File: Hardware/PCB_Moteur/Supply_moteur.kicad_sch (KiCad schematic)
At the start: 26 parts, among them J15 Vin_XT30PW-F, U13 L6981N33DR

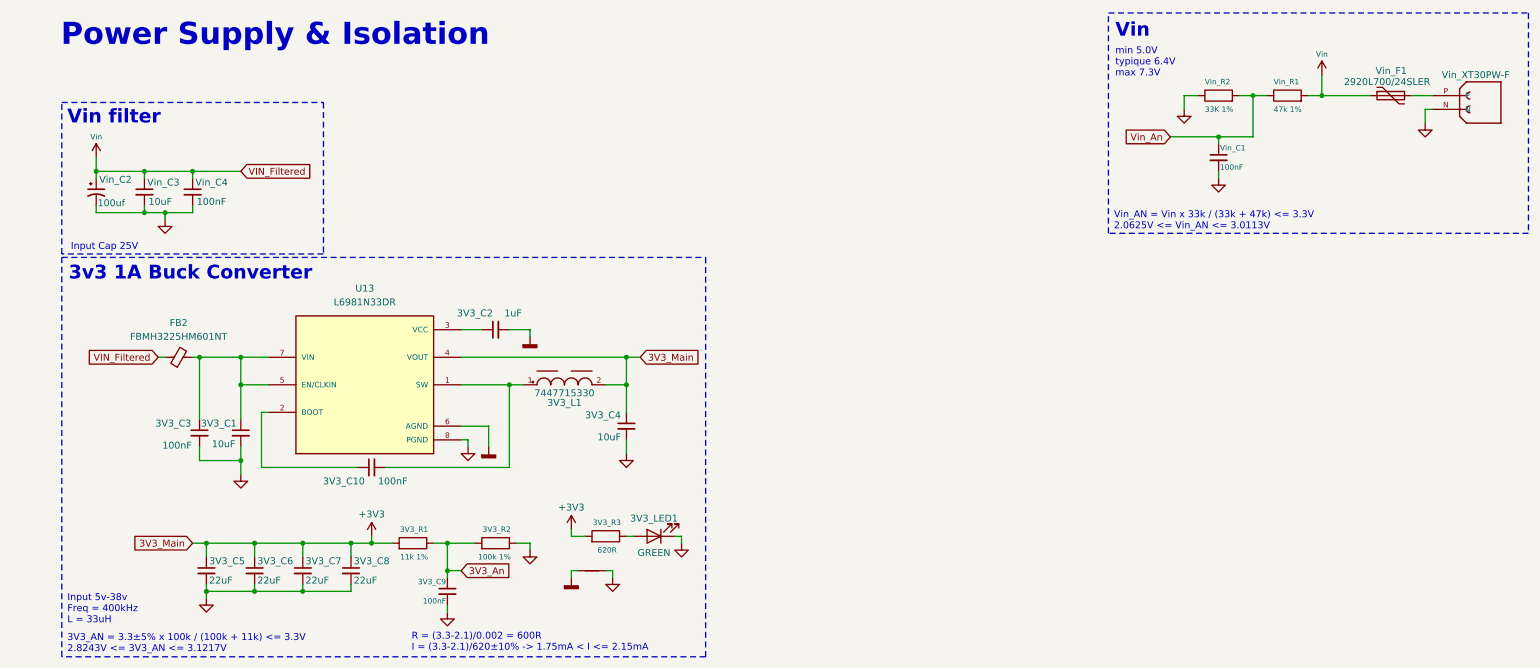
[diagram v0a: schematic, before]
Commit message: fix: LDO 5V SHDN + REFs (missing) + change EN valves controller connection + fix intrumental ampliop + add pull-down to sleep pins
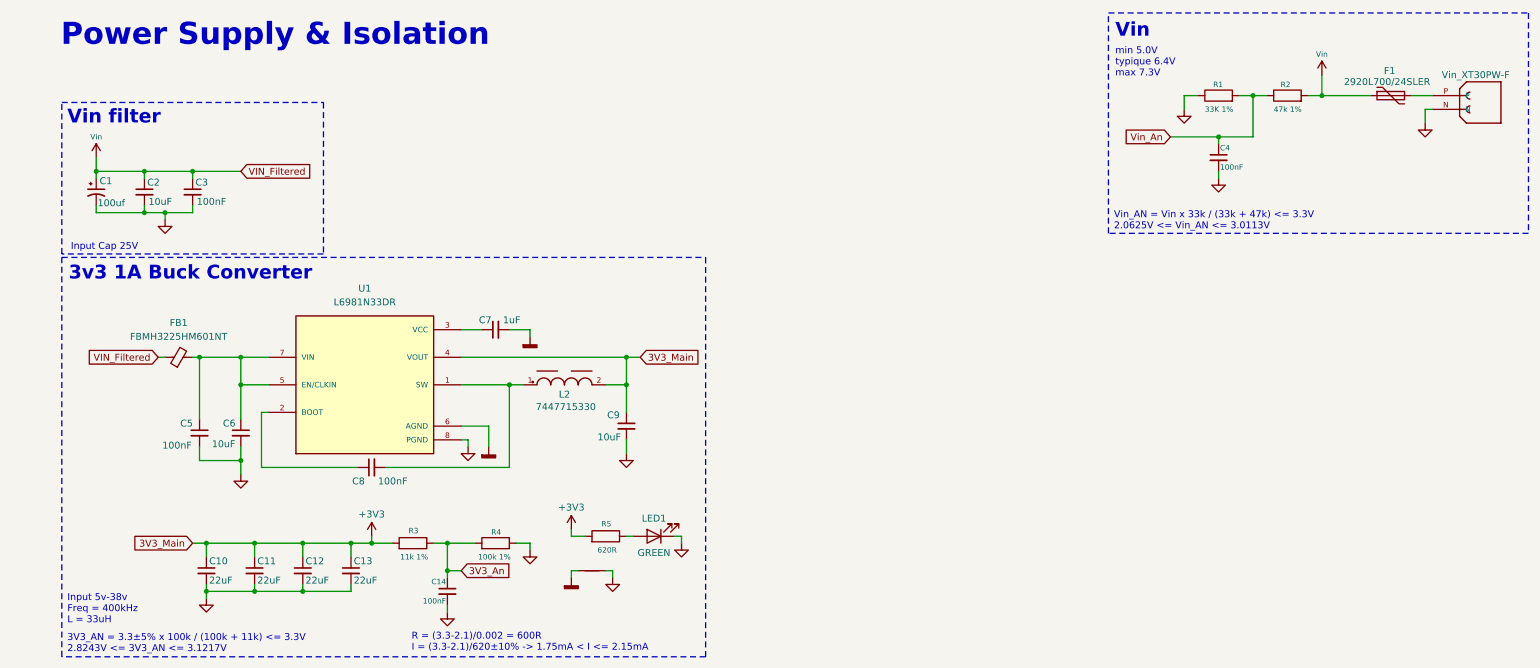
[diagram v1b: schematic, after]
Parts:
- renumbered Vin_C2 to C1, 3V3_C5 to C10, 3V3_C6 to C11, 3V3_C7 to C12, 3V3_C8 to C13, 3V3_C9 to C14, Vin_C3 to C2, Vin_C4 to C3, Vin_C1 to C4, 3V3_C3 to C5, 3V3_C1 to C6, 3V3_C2 to C7, 3V3_C10 to C8, 3V3_C4 to C9, Vin_F1 to F1, FB2 to FB1, J15 to J1, 3V3_L1 to L2, 3V3_LED1 to LED1, Vin_R2 to R1, Vin_R1 to R2, 3V3_R1 to R3, 3V3_R2 to R4, 3V3_R3 to R5, U13 to U1
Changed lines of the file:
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@@
 		(on_board yes)
 		(dnp no)
-		(property "Reference" "3V3_R2"
-			(at 96.774 107.95 90)
+		(property "Reference" "R4"
+			(at 94.996 108.458 90)
 			(effects
 				(font
@@
 			(project "PCB_moteur"
 				(path "/b0d87684-7b1c-41d8-8358-755aa327573e/92d1df5d-a307-4eea-a65c-ade4cb0ad548"
-					(reference "3V3_R2")
+					(reference "R4")
 					(unit 1)
 				)
@@
 		(on_board yes)
 		(dnp no)
-		(property "Reference" "3V3_C6"
+		(property "Reference" "C11"
 			(at 50.038 113.792 0)
 			(effects
@@
 			(project "PCB_moteur"
 				(path "/b0d87684-7b1c-41d8-8358-755aa327573e/92d1df5d-a307-4eea-a65c-ade4cb0ad548"
-					(reference "3V3_C6")
+					(reference "C11")
 					(unit 1)
 				)
@@
 		(on_board yes)
 		(dnp no)
-		(property "Reference" "3V3_R1"
-			(at 81.534 107.95 90)
+		(property "Reference" "R3"
+			(at 79.756 108.204 90)
 			(effects
 				(font
@@
 			(project "PCB_moteur"
 				(path "/b0d87684-7b1c-41d8-8358-755aa327573e/92d1df5d-a307-4eea-a65c-ade4cb0ad548"
-					(reference "3V3_R1")
+					(reference "R3")
 					(unit 1)
 				)
@@
 		(on_board yes)
 		(dnp no)
-		(property "Reference" "3V3_C1"
-			(at 39.624 88.392 0)
+		(property "Reference" "C6"
+			(at 43.688 88.392 0)
 			(effects
 				(font
@@
 			(project "PCB_moteur"
 				(path "/b0d87684-7b1c-41d8-8358-755aa327573e/92d1df5d-a307-4eea-a65c-ade4cb0ad548"
-					(reference "3V3_C1")
+					(reference "C6")
 					(unit 1)
 				)
@@
 		(on_board yes)
 		(dnp no)
-		(property "Reference" "3V3_C2"
-			(at 93.472 68.072 90)
+		(property "Reference" "C7"
+			(at 93.218 69.342 90)
 			(effects
 				(font
@@
 		)
 		(property "Value" "1uF"
-			(at 98.806 68.072 90)
+			(at 98.552 69.342 90)
 			(effects
 				(font
@@
 			(project "PCB_moteur"
 				(path "/b0d87684-7b1c-41d8-8358-755aa327573e/92d1df5d-a307-4eea-a65c-ade4cb0ad548"
-					(reference "3V3_C2")
+					(reference "C7")
 					(unit 1)
 				)
@@
 		(on_board yes)
 		(dnp no)
-		(property "Reference" "3V3_L1"
-			(at 106.68 84.582 0)
+		(property "Reference" "L2"
+			(at 106.68 83.058 0)
 			(effects
 				(font
@@
 		)
 		(property "Value" "7447715330"
-			(at 106.68 82.804 0)
+			(at 106.934 85.344 0)
 			(effects
 				(font
@@
 			(project "PCB_moteur"
 				(path "/b0d87684-7b1c-41d8-8358-755aa327573e/92d1df5d-a307-4eea-a65c-ade4cb0ad548"
-					(reference "3V3_L1")
+					(reference "L2")
 					(unit 1)
 				)
@@
 		(on_board yes)
 		(dnp no)
-		(property "Reference" "3V3_R3"
-			(at 117.094 106.68 90)
+		(property "Reference" "R5"
+			(at 115.316 106.934 90)
 			(effects
 				(font
@@
 			(project "PCB_moteur"
 				(path "/b0d87684-7b1c-41d8-8358-755aa327573e/92d1df5d-a307-4eea-a65c-ade4cb0ad548"
-					(reference "3V3_R3")
+					(reference "R5")
 					(unit 1)
 				)
@@
 		(on_board yes)
 		(dnp no)
-		(property "Reference" "Vin_C2"
-			(at 23.876 43.434 0)
+		(property "Reference" "C1"
+			(at 22.098 43.688 0)
 			(effects
 				(font
@@
 			(project "PCB_moteur"
 				(path "/b0d87684-7b1c-41d8-8358-755aa327573e/92d1df5d-a307-4eea-a65c-ade4cb0ad548"
-					(reference "Vin_C2")
+					(reference "C1")
 					(unit 1)
 				)
@@
 		(on_board yes)
 		(dnp no)
-		(property "Reference" "3V3_LED1"
+		(property "Reference" "LED1"
 			(at 123.19 105.918 0)
 			(effects
@@
 			(project "PCB_moteur"
 				(path "/b0d87684-7b1c-41d8-8358-755aa327573e/92d1df5d-a307-4eea-a65c-ade4cb0ad548"
-					(reference "3V3_LED1")
+					(reference "LED1")
 					(unit 1)
 				)
@@
 		(on_board yes)
 		(dnp no)
-		(property "Reference" "Vin_R2"
-			(at 224.79 25.4 90)
+		(property "Reference" "R1"
+			(at 226.314 25.908 90)
 			(effects
 				(font
@@
 			(project "PCB_moteur"
 				(path "/b0d87684-7b1c-41d8-8358-755aa327573e/92d1df5d-a307-4eea-a65c-ade4cb0ad548"
-					(reference "Vin_R2")
+					(reference "R1")
 					(unit 1)
 				)
@@
 		(on_board yes)
 		(dnp no)
-		(property "Reference" "3V3_C5"
+		(property "Reference" "C10"
 			(at 41.148 113.792 0)
 			(effects
@@
 			(project "PCB_moteur"
 				(path "/b0d87684-7b1c-41d8-8358-755aa327573e/92d1df5d-a307-4eea-a65c-ade4cb0ad548"
-					(reference "3V3_C5")
+					(reference "C10")
 					(unit 1)
 				)
@@
 		(on_board yes)
 		(dnp no)
-		(property "Reference" "Vin_F1"
-			(at 256.286 23.368 90)
+		(property "Reference" "F1"
+			(at 257.81 23.368 90)
 			(effects
 				(font
@@
 			(project "PCB_moteur"
 				(path "/b0d87684-7b1c-41d8-8358-755aa327573e/92d1df5d-a307-4eea-a65c-ade4cb0ad548"
-					(reference "Vin_F1")
+					(reference "F1")
 					(unit 1)
 				)
@@
 		(dnp no)
 		(fields_autoplaced yes)
-		(property "Reference" "U13"
+		(property "Reference" "U1"
 			(at 69.85 63.5 0)
 			(effects
@@
 			(project "PCB_moteur"
 				(path "/b0d87684-7b1c-41d8-8358-755aa327573e/92d1df5d-a307-4eea-a65c-ade4cb0ad548"
-					(reference "U13")
+					(reference "U1")
 					(unit 1)
 				)
@@
 		(on_board yes)
 		(dnp no)
-		(property "Reference" "Vin_R1"
-			(at 237.49 25.4 90)
+		(property "Reference" "R2"
+			(at 238.76 25.908 90)
 			(effects
 				(font
@@
 			(project "PCB_moteur"
 				(path "/b0d87684-7b1c-41d8-8358-755aa327573e/92d1df5d-a307-4eea-a65c-ade4cb0ad548"
-					(reference "Vin_R1")
+					(reference "R2")
 					(unit 1)
 				)
@@
 		(on_board yes)
 		(dnp no)
-		(property "Reference" "3V3_C9"
+		(property "Reference" "C14"
 			(at 84.836 117.602 0)
 			(effects
@@
 			(project "PCB_moteur"
 				(path "/b0d87684-7b1c-41d8-8358-755aa327573e/92d1df5d-a307-4eea-a65c-ade4cb0ad548"
-					(reference "3V3_C9")
+					(reference "C14")
 					(unit 1)
 				)
@@
 		(on_board yes)
 		(dnp no)
-		(property "Reference" "Vin_C1"
+		(property "Reference" "C4"
 			(at 227.584 37.592 0)
 			(effects
@@
 			(project "PCB_moteur"
 				(path "/b0d87684-7b1c-41d8-8358-755aa327573e/92d1df5d-a307-4eea-a65c-ade4cb0ad548"
-					(reference "Vin_C1")
+					(reference "C4")
 					(unit 1)
 				)
@@
 		(on_board yes)
 		(dnp no)
-		(property "Reference" "3V3_C4"
-			(at 110.49 86.868 0)
+		(property "Reference" "C9"
+			(at 114.554 86.868 0)
 			(effects
 				(font
@@
 			(project "PCB_moteur"
 				(path "/b0d87684-7b1c-41d8-8358-755aa327573e/92d1df5d-a307-4eea-a65c-ade4cb0ad548"
-					(reference "3V3_C4")
+					(reference "C9")
 					(unit 1)
 				)
@@
 		(on_board yes)
 		(dnp no)
-		(property "Reference" "Vin_C3"
+		(property "Reference" "C2"
 			(at 29.718 43.942 0)
 			(effects
@@
 			(project "PCB_moteur"
 				(path "/b0d87684-7b1c-41d8-8358-755aa327573e/92d1df5d-a307-4eea-a65c-ade4cb0ad548"
-					(reference "Vin_C3")
+					(reference "C2")
 					(unit 1)
 				)
@@
 		(on_board yes)
 		(dnp no)
-		(property "Reference" "J15"
+		(property "Reference" "J1"
 			(at 280.67 27.9399 0)
 			(effects
@@
 			(project "PCB_moteur"
 				(path "/b0d87684-7b1c-41d8-8358-755aa327573e/92d1df5d-a307-4eea-a65c-ade4cb0ad548"
-					(reference "J15")
+					(reference "J1")
 					(unit 1)
 				)
@@
 		(dnp no)
 		(fields_autoplaced yes)
-		(property "Reference" "FB2"
+		(property "Reference" "FB1"
 			(at 35.5219 69.85 90)
 			(effects
@@
 			(project "PCB_moteur"
 				(path "/b0d87684-7b1c-41d8-8358-755aa327573e/92d1df5d-a307-4eea-a65c-ade4cb0ad548"
-					(reference "FB2")
+					(reference "FB1")
 					(unit 1)
 				)
@@
 		(on_board yes)
 		(dnp no)
-		(property "Reference" "3V3_C10"
+		(property "Reference" "C8"
 			(at 69.85 99.06 90)
 			(effects
@@
 			(project "PCB_moteur"
 				(path "/b0d87684-7b1c-41d8-8358-755aa327573e/92d1df5d-a307-4eea-a65c-ade4cb0ad548"
-					(reference "3V3_C10")
+					(reference "C8")
 					(unit 1)
 				)
@@
 		(on_board yes)
 		(dnp no)
-		(property "Reference" "3V3_C3"
-			(at 31.242 88.392 0)
+		(property "Reference" "C5"
+			(at 35.814 88.392 0)
 			(effects
 				(font
@@
 			(project "PCB_moteur"
 				(path "/b0d87684-7b1c-41d8-8358-755aa327573e/92d1df5d-a307-4eea-a65c-ade4cb0ad548"
-					(reference "3V3_C3")
+					(reference "C5")
 					(unit 1)
 				)
@@
 		(on_board yes)
 		(dnp no)
-		(property "Reference" "Vin_C4"
+		(property "Reference" "C3"
 			(at 38.608 43.942 0)
 			(effects
@@
 			(project "PCB_moteur"
 				(path "/b0d87684-7b1c-41d8-8358-755aa327573e/92d1df5d-a307-4eea-a65c-ade4cb0ad548"
-					(reference "Vin_C4")
+					(reference "C3")
 					(unit 1)
 				)
@@
 		(on_board yes)
 		(dnp no)
-		(property "Reference" "3V3_C7"
+		(property "Reference" "C12"
 			(at 58.928 113.792 0)
 			(effects
@@
 			(project "PCB_moteur"
 				(path "/b0d87684-7b1c-41d8-8358-755aa327573e/92d1df5d-a307-4eea-a65c-ade4cb0ad548"
-					(reference "3V3_C7")
+					(reference "C12")
 					(unit 1)
 				)
@@
 		(on_board yes)
 		(dnp no)
-		(property "Reference" "3V3_C8"
+		(property "Reference" "C13"
 			(at 67.818 113.792 0)
 			(effects
@@
 			(project "PCB_moteur"
 				(path "/b0d87684-7b1c-41d8-8358-755aa327573e/92d1df5d-a307-4eea-a65c-ade4cb0ad548"
-					(reference "3V3_C8")
+					(reference "C13")
 					(unit 1)
 				)

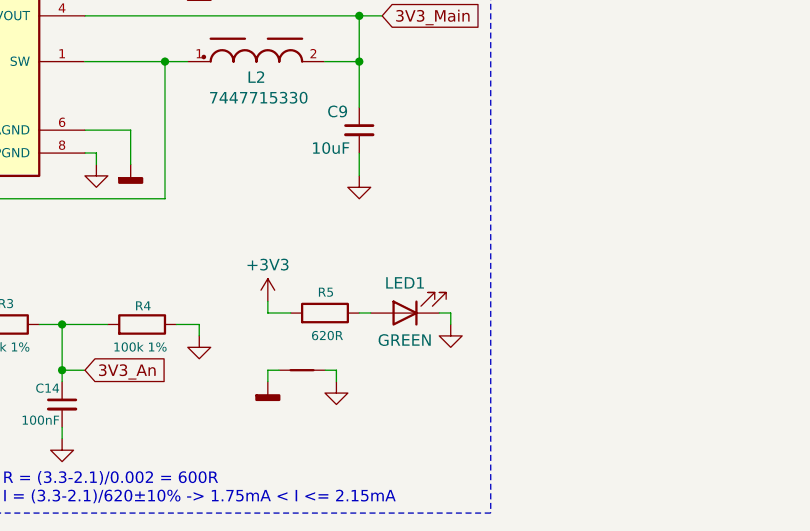
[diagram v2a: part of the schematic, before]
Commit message: wip : minor corrections and fix footprints except connectors
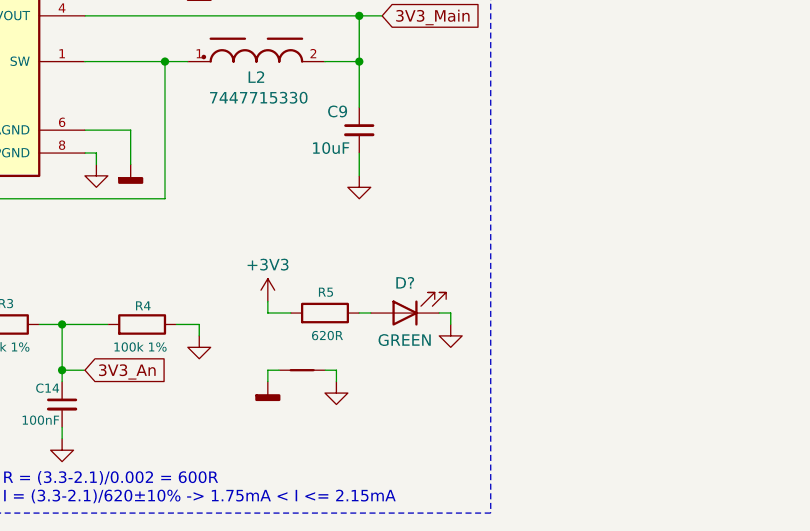
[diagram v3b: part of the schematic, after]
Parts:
- removed LED1: GREEN, LED_SMD:LED_0603_1608Metric, symbol Device:LED
- added D?: GREEN, ODB:LED_QBLP601-AG15, symbol Device:LED
- C1: footprint ODB:WCAP-PSHP_8X8.7_DXL_ -> pcb_moteur:WCAP-PSHP_8X8.7_DXL_
- C14, C3, C4, C5, C6, C7, C8: footprint Capacitor_SMD:C_0603_1608Metric -> Capacitor_SMD:C_0805_2012Metric
- C2, C9: footprint Capacitor_SMD:C_1210_3225Metric -> Capacitor_SMD:C_0805_2012Metric
- L2: footprint ODB:WE-PD_1245 -> pcb_moteur:WE-PD_1245
- U1: footprint ODB:SOIC127P600X175-8N -> pcb_moteur:SOIC127P600X175-8N
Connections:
- net GND: now also D?.1 (K)
- net at R5.1: now also D?.2 (A)
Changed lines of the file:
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@@
+	)
+	(symbol
+		(lib_id "Device:LED")
+		(at 123.19 109.22 180)
+		(unit 1)
+		(exclude_from_sim no)
+		(in_bom yes)
+		(on_board yes)
+		(dnp no)
+		(property "Reference" "D?"
+			(at 123.19 105.918 0)
+			(effects
+				(font
+					(size 1.27 1.27)
+				)
+			)
+		)
+		(property "Value" "GREEN"
+			(at 123.19 112.268 0)
+			(effects
+				(font
+					(size 1.27 1.27)
+				)
+			)
+		)
+		(property "Footprint" "ODB:LED_QBLP601-AG15"
+			(at 123.19 109.22 0)
+			(effects
+				(font
+					(size 1.27 1.27)
+				)
+				(hide yes)
+			)
+		)
+		(property "Datasheet" "https://www.digikey.ca/en/products/detail/qt-brightek-qtb/QBLP601-AG15/16499667"
+			(at 123.19 109.22 0)
+			(effects
+				(font
+					(size 1.27 1.27)
+				)
+				(hide yes)
+			)
+		)
+		(property "Description" "Light emitting diode"
+			(at 123.19 109.22 0)
+			(effects
+				(font
+					(size 1.27 1.27)
+				)
+				(hide yes)
+			)
+		)
+		(property "DigiKey_Part_Number" "1516-QBLP601-AG15CT-ND"
+			(at 123.19 109.22 0)
+			(effects
+				(font
+					(size 1.27 1.27)
+				)
+				(hide yes)
+			)
+		)
+		(property "Purchase-URL" ""
+			(at 123.19 109.22 0)
+			(effects
+				(font
+					(size 1.27 1.27)
+				)
+				(hide yes)
+			)
+		)
+		(property "Sim.Device" ""
+			(at 123.19 109.22 0)
+			(effects
+				(font
+					(size 1.27 1.27)
+				)
+				(hide yes)
+			)
+		)
+		(property "Sim.Pins" ""
+			(at 123.19 109.22 0)
+			(effects
+				(font
+					(size 1.27 1.27)
+				)
+				(hide yes)
+			)
+		)
+		(property "Sim.Type" ""
+			(at 123.19 109.22 0)
+			(effects
+				(font
+					(size 1.27 1.27)
+				)
+				(hide yes)
+			)
+		)
+		(property "Manufacturer_Part_Number" "QBLP601-AG15"
+			(at 123.19 109.22 0)
+			(effects
+				(font
+					(size 1.27 1.27)
+				)
+				(hide yes)
+			)
+		)
+		(pin "1"
+		)
+		(pin "2"
+		)
+		(instances
+			(project "PCB_moteur"
+				(path "/b0d87684-7b1c-41d8-8358-755aa327573e/92d1df5d-a307-4eea-a65c-ade4cb0ad548"
+					(reference "D?")
+					(unit 1)
+				)
+			)
+		)
 	)
 	(symbol
@@
 			)
 		)
-		(property "Footprint" "Capacitor_SMD:C_0603_1608Metric"
+		(property "Footprint" "Capacitor_SMD:C_0805_2012Metric"
 			(at 46.99 90.17 0)
 			(effects
@@
 			)
 		)
-		(property "Footprint" "Capacitor_SMD:C_0603_1608Metric"
+		(property "Footprint" "Capacitor_SMD:C_0805_2012Metric"
 			(at 93.98 71.12 0)
 			(effects
@@
 			)
 		)
-		(property "Footprint" "ODB:WE-PD_1245"
+		(property "Footprint" "pcb_moteur:WE-PD_1245"
 			(at 106.68 81.28 0)
 			(effects
@@
 			)
 		)
-		(property "Footprint" "ODB:WCAP-PSHP_8X8.7_DXL_"
+		(property "Footprint" "pcb_moteur:WCAP-PSHP_8X8.7_DXL_"
 			(at 20.32 45.72 0)
 			(effects
@@
 	)
 	(symbol
-		(lib_id "Device:LED")
-		(at 123.19 109.22 180)
-		(unit 1)
-		(exclude_from_sim no)
-		(in_bom yes)
-		(on_board yes)
-		(dnp no)
-		(property "Reference" "LED1"
-			(at 123.19 105.918 0)
-			(effects
-				(font
-					(size 1.27 1.27)
-				)
-			)
-		)
-		(property "Value" "GREEN"
-			(at 123.19 112.268 0)
-			(effects
-				(font
-					(size 1.27 1.27)
-				)
-			)
-		)
-		(property "Footprint" "LED_SMD:LED_0603_1608Metric"
-			(at 123.19 109.22 0)
-			(effects
-				(font
-					(size 1.27 1.27)
-				)
-				(hide yes)
-			)
-		)
-		(property "Datasheet" "~"
-			(at 123.19 109.22 0)
-			(effects
-				(font
-					(size 1.27 1.27)
-				)
-				(hide yes)
-			)
-		)
-		(property "Description" "Light emitting diode"
-			(at 123.19 109.22 0)
-			(effects
-				(font
-					(size 1.27 1.27)
-				)
-				(hide yes)
-			)
-		)
-		(pin "1"
-		)
-		(pin "2"
-		)
-		(instances
-			(project "PCB_moteur"
-				(path "/b0d87684-7b1c-41d8-8358-755aa327573e/92d1df5d-a307-4eea-a65c-ade4cb0ad548"
-					(reference "LED1")
-					(unit 1)
-				)
-			)
-		)
-	)
-	(symbol
 		(lib_id "power:GND")
 		(at 33.02 50.8 0)
@@
 			)
 		)
-		(property "Footprint" "ODB:SOIC127P600X175-8N"
+		(property "Footprint" "pcb_moteur:SOIC127P600X175-8N"
 			(at 69.85 81.28 0)
 			(effects
@@
 			)
 		)
-		(property "Footprint" "Capacitor_SMD:C_0603_1608Metric"
+		(property "Footprint" "Capacitor_SMD:C_0805_2012Metric"
 			(at 85.09 119.38 0)
 			(effects
@@
 			)
 		)
-		(property "Footprint" "Capacitor_SMD:C_0603_1608Metric"
+		(property "Footprint" "Capacitor_SMD:C_0805_2012Metric"
 			(at 227.33 39.37 0)
 			(effects
@@
 			)
 		)
-		(property "Footprint" "Capacitor_SMD:C_1210_3225Metric"
+		(property "Footprint" "Capacitor_SMD:C_0805_2012Metric"
 			(at 118.11 88.9 0)
 			(effects
@@
 			)
 		)
-		(property "Footprint" "Capacitor_SMD:C_1210_3225Metric"
+		(property "Footprint" "Capacitor_SMD:C_0805_2012Metric"
 			(at 29.21 45.72 0)
 			(effects
@@
 			)
 		)
-		(property "Footprint" "Capacitor_SMD:C_0603_1608Metric"
+		(property "Footprint" "Capacitor_SMD:C_0805_2012Metric"
 			(at 71.12 96.52 0)
 			(effects
@@
 			)
 		)
-		(property "Footprint" "Capacitor_SMD:C_0603_1608Metric"
+		(property "Footprint" "Capacitor_SMD:C_0805_2012Metric"
 			(at 39.37 90.17 0)
 			(effects
@@
 			)
 		)
-		(property "Footprint" "Capacitor_SMD:C_0603_1608Metric"
+		(property "Footprint" "Capacitor_SMD:C_0805_2012Metric"
 			(at 38.1 45.72 0)
 			(effects
